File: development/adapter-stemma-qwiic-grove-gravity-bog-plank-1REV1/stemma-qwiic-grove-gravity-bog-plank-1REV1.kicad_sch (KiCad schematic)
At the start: 13 parts, among them J1 SM04B-SRSS-TB (HC-1.0-4PWT), J10 ED10BGFBK, J11 Conn_01x10, J12 Conn_01x10, J2 SM04B-SRSS-TB (HC-1.0-4PWT), J3 SM04B-SRSS-TB (HC-1.0-4PWT), J4 SM04B-SRSS-TB (HC-1.0-4PWT), J6 S4B-PH-SM4-TB (HC-PH-4AWT), J7 S3B-PH-SM4-TB (HC-PH-3AWT), J8 S4B-PH-SM4-TB (HC-PH-4AWT), J9 HY-4P

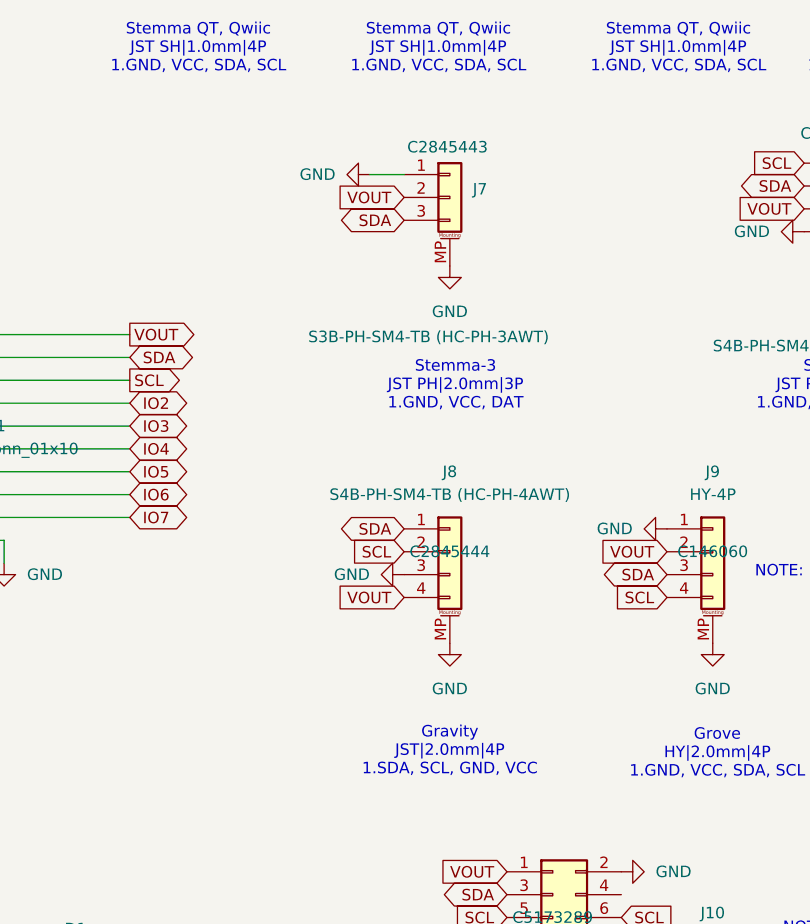
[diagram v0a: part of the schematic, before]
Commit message: Change pinout on I2C quick connect
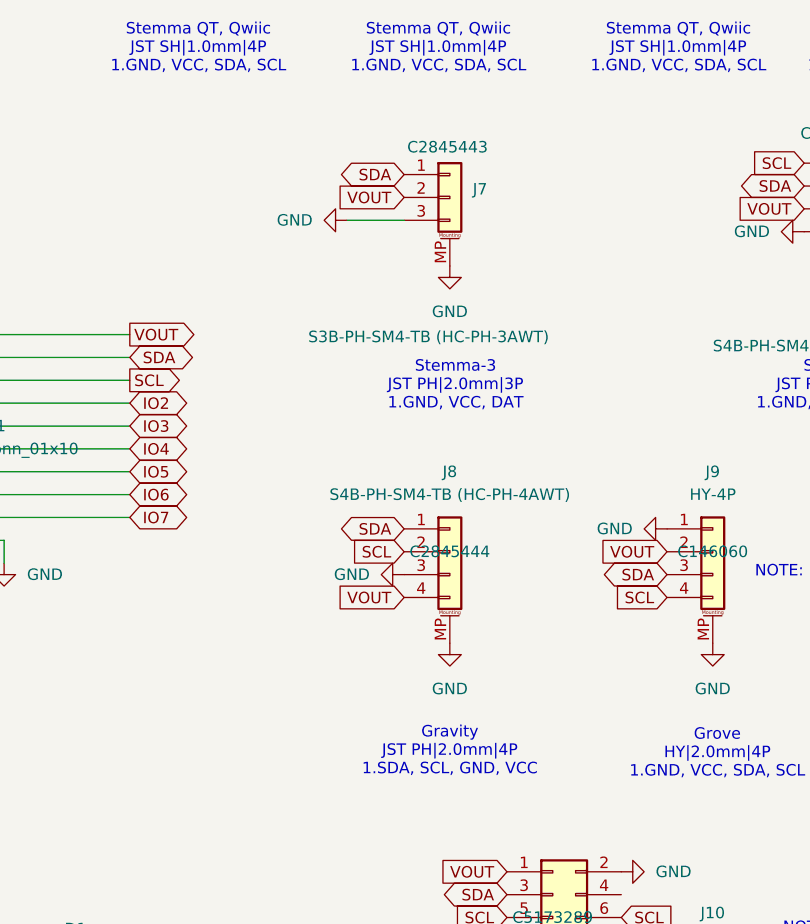
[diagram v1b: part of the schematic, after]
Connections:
- net GND: now also J7.3 (Pin_3); no longer J7.1 (Pin_1)
- net SDA: now also J7.1 (Pin_1); no longer J7.3 (Pin_3)
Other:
- note added: "Gravity JST PH|2.0mm|4P 1.SDA, SCL, GND, VCC"
- note removed: "Gravity JST|2.0mm|4P 1.SDA, SCL, GND, VCC"
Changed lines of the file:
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@@
 	(generator_version "9.0")
 	(paper "A4")
-	(text "Gravity\nJST|2.0mm|4P\n1.SDA, SCL, GND, VCC"
+	(text "Gravity\nJST PH|2.0mm|4P\n1.SDA, SCL, GND, VCC"
 		(exclude_from_sim no)
 		(at 100.33 130.175 0)
@@
 	(wire
 		(pts
-			(xy 91.44 66.04) (xy 95.25 66.04)
+			(xy 40.64 96.52) (xy 64.77 96.52)
 		)
 		(stroke
@@
 	(wire
 		(pts
-			(xy 40.64 96.52) (xy 64.77 96.52)
+			(xy 40.64 104.14) (xy 64.77 104.14)
 		)
 		(stroke
@@
 	(wire
 		(pts
-			(xy 40.64 104.14) (xy 64.77 104.14)
+			(xy 40.64 93.98) (xy 64.77 93.98)
 		)
 		(stroke
@@
 	(wire
 		(pts
-			(xy 40.64 93.98) (xy 64.77 93.98)
+			(xy 40.64 104.14) (xy 39.37 104.14)
 		)
 		(stroke
@@
 	(wire
 		(pts
-			(xy 40.64 104.14) (xy 39.37 104.14)
+			(xy 88.9 71.12) (xy 95.25 71.12)
 		)
 		(stroke
@@
 	(global_label "SDA"
 		(shape bidirectional)
-		(at 95.25 71.12 180)
+		(at 95.25 66.04 180)
 		(fields_autoplaced yes)
 		(effects
@@
 		)
 		(property "Intersheetrefs" "${INTERSHEET_REFS}"
-			(at 87.5854 71.12 0)
+			(at 87.5854 66.04 0)
 			(effects
 				(font
@@
 	(symbol
 		(lib_id "power:GND")
-		(at 91.44 66.04 270)
+		(at 88.9 71.12 270)
 		(unit 1)
 		(exclude_from_sim no)
@@
 		(fields_autoplaced yes)
 		(property "Reference" "#PWR08"
-			(at 85.09 66.04 0)
+			(at 82.55 71.12 0)
 			(effects
 				(font
@@
 		)
 		(property "Value" "GND"
-			(at 87.63 66.0399 90)
+			(at 85.09 71.1199 90)
 			(effects
 				(font
@@
 		)
 		(property "Footprint" ""
-			(at 91.44 66.04 0)
+			(at 88.9 71.12 0)
 			(effects
 				(font
@@
 		)
 		(property "Datasheet" ""
-			(at 91.44 66.04 0)
+			(at 88.9 71.12 0)
 			(effects
 				(font
@@
 		)
 		(property "Description" ""
-			(at 91.44 66.04 0)
+			(at 88.9 71.12 0)
 			(effects
 				(font

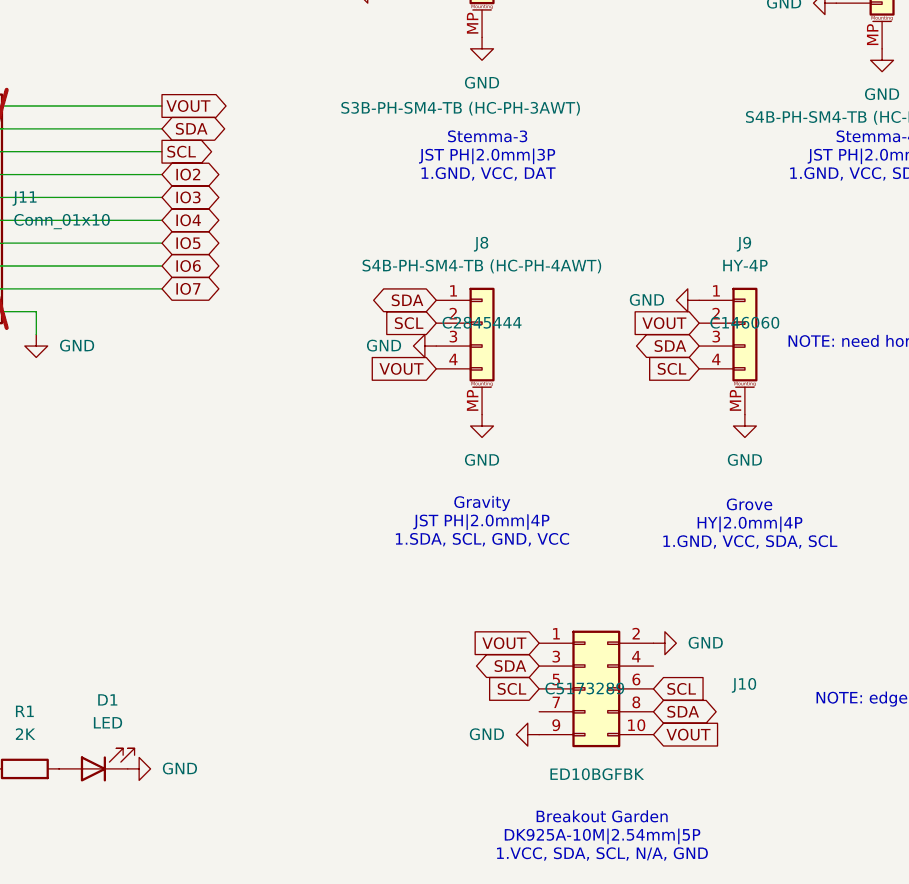
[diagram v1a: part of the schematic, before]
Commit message: 7R2 with vout protection
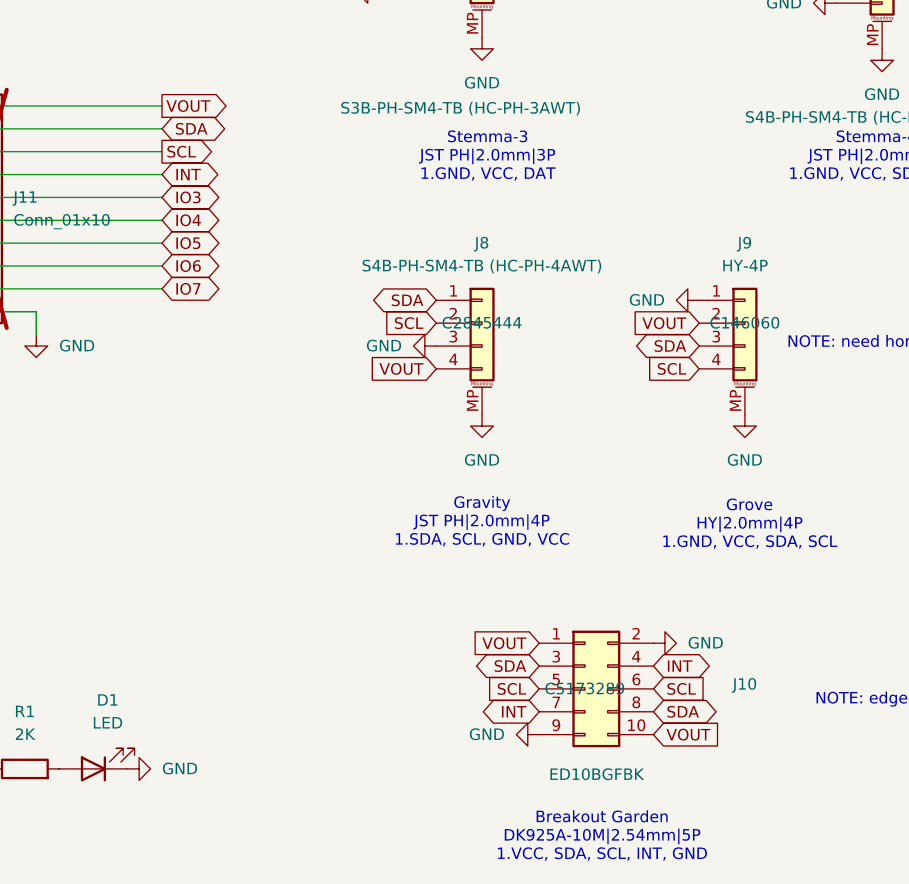
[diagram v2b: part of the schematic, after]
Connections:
- net IO2 is gone; now on net INT: J11.4 (Pin_4), J12.4 (Pin_4)
- net INT: now reaches J10.4 (Pin_4)
- net INT: now also J10.7 (Pin_7)
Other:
- note added: "Breakout Garden DK925A-10M|2.54mm|5P 1.VCC, SDA, SCL, INT, GND"
- note removed: "Breakout Garden DK925A-10M|2.54mm|5P 1.VCC, SDA, SCL, N/A, GND"
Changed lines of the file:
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@@
 		)
 	)
-	(text "Breakout Garden\nDK925A-10M|2.54mm|5P\n1.VCC, SDA, SCL, N/A, GND"
+	(text "Breakout Garden\nDK925A-10M|2.54mm|5P\n1.VCC, SDA, SCL, INT, GND"
 		(exclude_from_sim no)
 		(at 113.665 165.1 0)
@@
 		)
 	)
-	(global_label "IO2"
+	(global_label "INT"
 		(shape bidirectional)
 		(at 64.77 91.44 0)
@@
 		)
 		(property "Intersheetrefs" "${INTERSHEET_REFS}"
-			(at 72.0113 91.44 0)
+			(at 71.7694 91.44 0)
 			(effects
 				(font
@@
 				)
 				(justify right)
+				(hide yes)
+			)
+		)
+	)
+	(global_label "INT"
+		(shape bidirectional)
+		(at 119.38 146.05 0)
+		(fields_autoplaced yes)
+		(effects
+			(font
+				(size 1.27 1.27)
+			)
+			(justify left)
+		)
+		(property "Intersheetrefs" "${INTERSHEET_REFS}"
+			(at 126.3794 146.05 0)
+			(effects
+				(font
+					(size 1.27 1.27)
+				)
+				(justify left)
 				(hide yes)
 			)
@@
 				(hide yes)
 			)
+		)
+	)
+	(global_label "INT"
+		(shape bidirectional)
+		(at 106.68 151.13 180)
+		(fields_autoplaced yes)
+		(effects
+			(font
+				(size 1.27 1.27)
+			)
+			(justify right)
+		)
+		(property "Intersheetrefs" "${INTERSHEET_REFS}"
+			(at 99.6806 151.13 0)
+			(effects
+				(font
+					(size 1.27 1.27)
+				)
+				(justify right)
+				(hide yes)
+			)
